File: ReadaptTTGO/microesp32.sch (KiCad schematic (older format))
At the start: 41 parts, among them J3 Micro_SD_Card, J4 Conn_01x13_Female, J5 Conn_01x13_Female, SW2 SW_Push, U2 ESP32

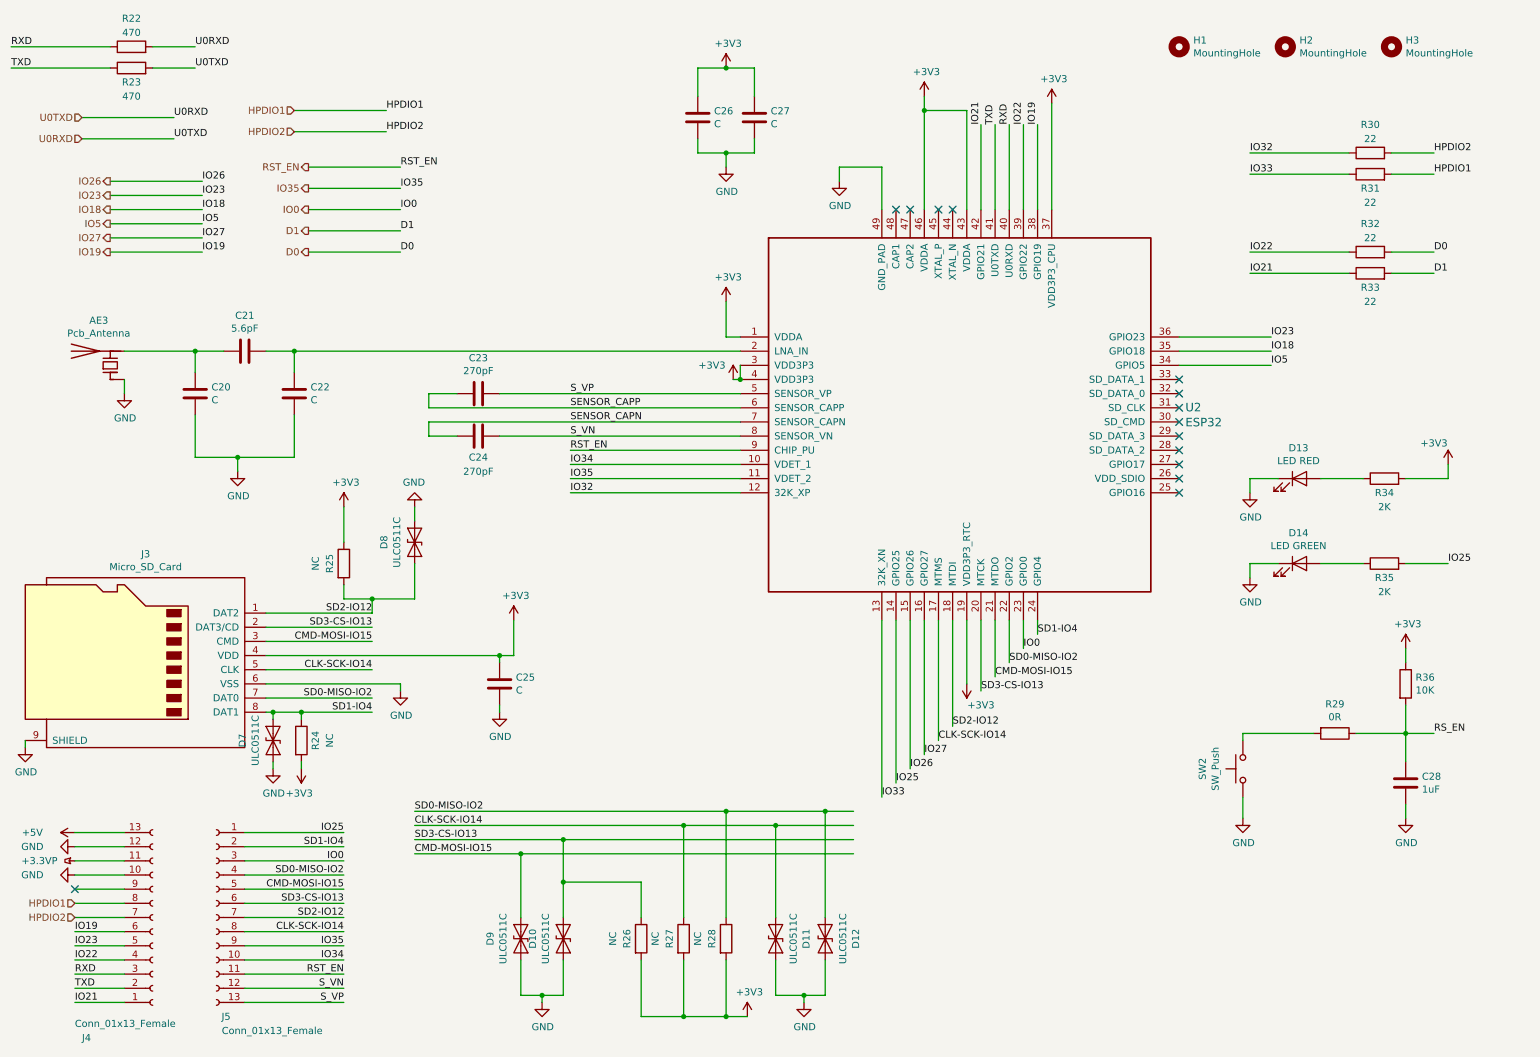
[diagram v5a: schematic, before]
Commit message: PCB sin traces
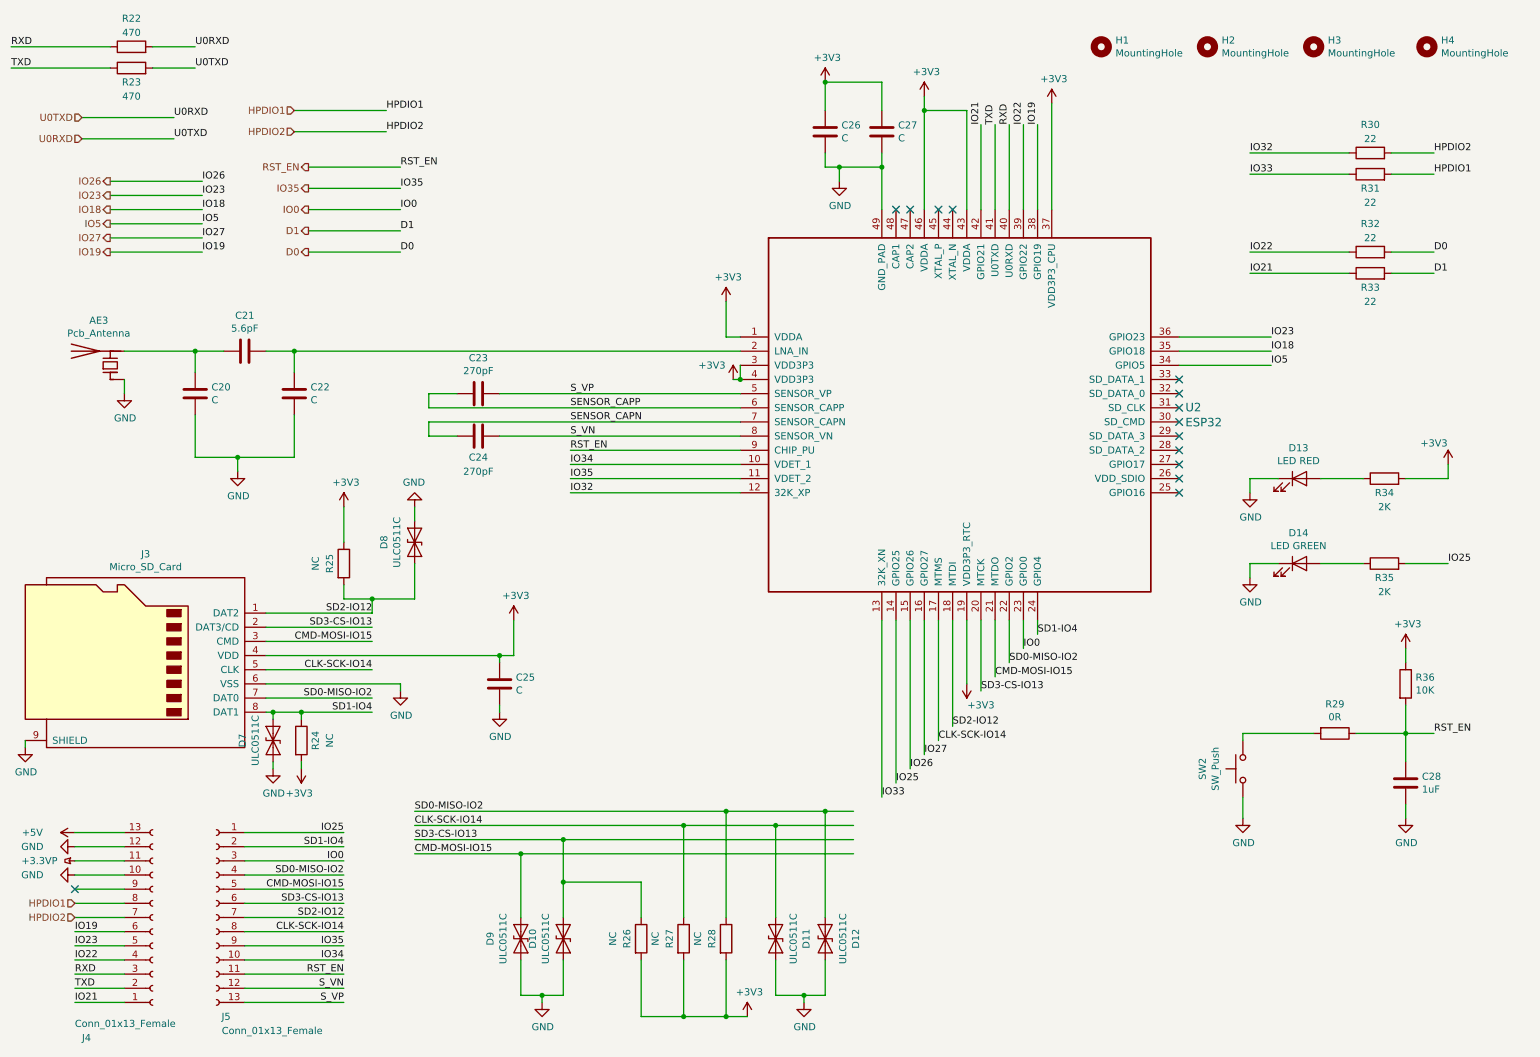
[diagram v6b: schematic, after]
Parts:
- added H4: MountingHole, Fiducial:Fiducial_1mm_Mask2mm, symbol Mechanical:MountingHole
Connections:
- net RS_EN is gone; now on net RST_EN: C28.1, R29.1, R36.2
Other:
- moved on the sheet: C26, C27, H1, H2, H3
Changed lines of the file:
@@
 L power:+3V3 #PWR0162
 U 1 1 5D1B42AD
-P 5600 900
-F 0 "#PWR0162" H 5600 750 50  0001 C CNN
-F 1 "+3V3" H 5615 1073 50  0000 C CNN
-F 2 "" H 5600 900 50  0001 C CNN
-F 3 "" H 5600 900 50  0001 C CNN
-	1    5600 900
+P 6300 1000
+F 0 "#PWR0162" H 6300 850 50  0001 C CNN
+F 1 "+3V3" H 6315 1173 50  0000 C CNN
+F 2 "" H 6300 1000 50  0001 C CNN
+F 3 "" H 6300 1000 50  0001 C CNN
+	1    6300 1000
 	1    0    0    -1
 $EndComp
@@
 L Device:C C26
 U 1 1 5D1B89DC
-P 5400 1250
-F 0 "C26" H 5515 1296 50  0000 L CNN
-F 1 "C" H 5515 1205 50  0000 L CNN
-F 2 "Capacitor_SMD:C_0201_0603Metric" H 5438 1100 50  0001 C CNN
-F 3 "~" H 5400 1250 50  0001 C CNN
-	1    5400 1250
+P 6300 1350
+F 0 "C26" H 6415 1396 50  0000 L CNN
+F 1 "C" H 6415 1305 50  0000 L CNN
+F 2 "Capacitor_SMD:C_0201_0603Metric" H 6338 1200 50  0001 C CNN
+F 3 "~" H 6300 1350 50  0001 C CNN
+	1    6300 1350
 	1    0    0    -1
 $EndComp
@@
 L Device:C C27
 U 1 1 5D1B9274
-P 5800 1250
-F 0 "C27" H 5915 1296 50  0000 L CNN
-F 1 "C" H 5915 1205 50  0000 L CNN
-F 2 "Capacitor_SMD:C_01005_0402Metric" H 5838 1100 50  0001 C CNN
-F 3 "~" H 5800 1250 50  0001 C CNN
-	1    5800 1250
-	1    0    0    -1
-$EndComp
-$Comp
-L power:GND #PWR0163
-U 1 1 5D1BB8F4
-P 5600 1600
-F 0 "#PWR0163" H 5600 1350 50  0001 C CNN
-F 1 "GND" H 5605 1427 50  0000 C CNN
-F 2 "" H 5600 1600 50  0001 C CNN
-F 3 "" H 5600 1600 50  0001 C CNN
-	1    5600 1600
-	1    0    0    -1
-$EndComp
-Wire Wire Line
-	5400 1500 5600 1500
-Wire Wire Line
-	5600 1600 5600 1500
+P 6700 1350
+F 0 "C27" H 6815 1396 50  0000 L CNN
+F 1 "C" H 6815 1305 50  0000 L CNN
+F 2 "Capacitor_SMD:C_01005_0402Metric" H 6738 1200 50  0001 C CNN
+F 3 "~" H 6700 1350 50  0001 C CNN
+	1    6700 1350
+	1    0    0    -1
+$EndComp
+Wire Wire Line
+	6300 1600 6400 1600
 $Comp
 L Device:C C23
@@
 Wire Wire Line
 	5650 3100 5700 3100
-Connection ~ 5600 1500
-Wire Wire Line
-	5600 1500 5800 1500
-Wire Wire Line
-	5800 1500 5800 1400
-Wire Wire Line
-	5400 1500 5400 1400
-Wire Wire Line
-	5800 900  5800 1100
-Wire Wire Line
-	5400 900  5400 1100
-Connection ~ 5600 900
-Wire Wire Line
-	5600 900  5800 900
-Wire Wire Line
-	5400 900  5600 900
+Wire Wire Line
+	6700 1600 6700 1500
+Wire Wire Line
+	6300 1600 6300 1500
+Wire Wire Line
+	6700 1000 6700 1200
+Wire Wire Line
+	6300 1000 6300 1200
 $Comp
 L power:GND #PWR0165
@@
 Wire Wire Line
 	6700 1900 6700 1600
-Wire Wire Line
-	6700 1600 6400 1600
 $Comp
 L power:+3V3 #PWR0166
@@
 	10400 5100 10400 5000
 Text Label 10600 5600 0    50   ~ 0
-RS_EN
+RST_EN
 $Comp
 L Mechanical:MountingHole H1
 U 1 1 5D2425E0
-P 8800 750
-F 0 "H1" H 8900 796 50  0000 L CNN
-F 1 "MountingHole" H 8900 705 50  0000 L CNN
-F 2 "Fiducial:Fiducial_1mm_Mask2mm" H 8800 750 50  0001 C CNN
-F 3 "~" H 8800 750 50  0001 C CNN
-	1    8800 750
+P 8250 750
+F 0 "H1" H 8350 796 50  0000 L CNN
+F 1 "MountingHole" H 8350 705 50  0000 L CNN
+F 2 "Fiducial:Fiducial_1mm_Mask2mm" H 8250 750 50  0001 C CNN
+F 3 "~" H 8250 750 50  0001 C CNN
+	1    8250 750
 	1    0    0    -1
 $EndComp
@@
 L Mechanical:MountingHole H2
 U 1 1 5D24333A
-P 9550 750
-F 0 "H2" H 9650 796 50  0000 L CNN
-F 1 "MountingHole" H 9650 705 50  0000 L CNN
-F 2 "Fiducial:Fiducial_1mm_Mask2mm" H 9550 750 50  0001 C CNN
-F 3 "~" H 9550 750 50  0001 C CNN
-	1    9550 750
+P 9000 750
+F 0 "H2" H 9100 796 50  0000 L CNN
+F 1 "MountingHole" H 9100 705 50  0000 L CNN
+F 2 "Fiducial:Fiducial_1mm_Mask2mm" H 9000 750 50  0001 C CNN
+F 3 "~" H 9000 750 50  0001 C CNN
+	1    9000 750
 	1    0    0    -1
 $EndComp
@@
 L Mechanical:MountingHole H3
 U 1 1 5D906E62
-P 10300 750
-F 0 "H3" H 10400 796 50  0000 L CNN
-F 1 "MountingHole" H 10400 705 50  0000 L CNN
-F 2 "Fiducial:Fiducial_1mm_Mask2mm" H 10300 750 50  0001 C CNN
-F 3 "~" H 10300 750 50  0001 C CNN
-	1    10300 750
+P 9750 750
+F 0 "H3" H 9850 796 50  0000 L CNN
+F 1 "MountingHole" H 9850 705 50  0000 L CNN
+F 2 "Fiducial:Fiducial_1mm_Mask2mm" H 9750 750 50  0001 C CNN
+F 3 "~" H 9750 750 50  0001 C CNN
+	1    9750 750
 	1    0    0    -1
 $EndComp
@@
 Wire Wire Line
 	2550 2900 5700 2900
+Connection ~ 6400 1600
+Connection ~ 6700 1600
+Wire Wire Line
+	6400 1600 6700 1600
+Wire Wire Line
+	6300 1000 6700 1000
+Connection ~ 6300 1000
+$Comp
+L Mechanical:MountingHole H4
+U 1 1 5D296F29
+P 10550 750
+F 0 "H4" H 10650 796 50  0000 L CNN
+F 1 "MountingHole" H 10650 705 50  0000 L CNN
+F 2 "Fiducial:Fiducial_1mm_Mask2mm" H 10550 750 50  0001 C CNN
+F 3 "~" H 10550 750 50  0001 C CNN
+	1    10550 750
+	1    0    0    -1
+$EndComp
 $EndSCHEMATC

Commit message: Pre aplicacion de las zonas de relleno
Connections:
- net U0RXD: no longer R23.2
- new net U0TXD: R23.2
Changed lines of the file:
@@
 Text Label 1850 750  0    50   ~ 0
 U0RXD
+Text Label 1700 1250 0    50   ~ 0
+U0TXD
 Text Label 1700 1400 0    50   ~ 0
-U0TXD
-Text Label 1700 1250 0    50   ~ 0
 U0RXD
 Wire Wire Line

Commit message: PCB Para revision
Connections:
- net GND: now also U2.25 (GPIO16)
- no-connect marks 14 -> 13
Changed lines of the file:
@@
 	2600 5450 3100 5450
 NoConn ~ 1000 6700
-NoConn ~ 8800 3900
 NoConn ~ 8800 3700
 NoConn ~ 8800 3600
@@
 	1    0    0    -1
 $EndComp
+$Comp
+L power:GND #PWR?
+U 1 1 5D5A9AF7
+P 8800 4000
+F 0 "#PWR?" H 8800 3750 50  0001 C CNN
+F 1 "GND" H 8805 3827 50  0000 C CNN
+F 2 "" H 8800 4000 50  0001 C CNN
+F 3 "" H 8800 4000 50  0001 C CNN
+	1    8800 4000
+	1    0    0    -1
+$EndComp
+Wire Wire Line
+	8800 3900 8800 4000
 $EndSCHEMATC
